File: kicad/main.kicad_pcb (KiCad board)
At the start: 2 copper layers, 130.7 x 94.9 mm, 40 parts

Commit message: wip: routing
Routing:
- net P2: track 92.2 -> 93.3 mm
- added copper zone on B.Cu, net GND

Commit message: chore: finish routing
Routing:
- net GND: track 909.2 -> 997.3 mm
- net RAW: track 12.7 -> 38.3 mm
- net RST: track 39.0 -> 51.5 mm, vias 0 -> 1
- net pos: track 49.6 -> 52.2 mm, vias 1 -> 2
- net P0: track 48.3 -> 49.2 mm
- net P15: track 151.5 -> 152.1 mm

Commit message: chore: straighten paths
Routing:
- net GND: track 997.3 -> 961.0 mm
- net P14: track 133.1 -> 138.2 mm
- net P16: track 107.9 -> 110.3 mm
- net P15: track 152.1 -> 153.7 mm
- net P9: track 133.8 -> 134.5 mm
- net P4: track 138.9 -> 139.6 mm
- net P10: track 83.9 -> 83.3 mm

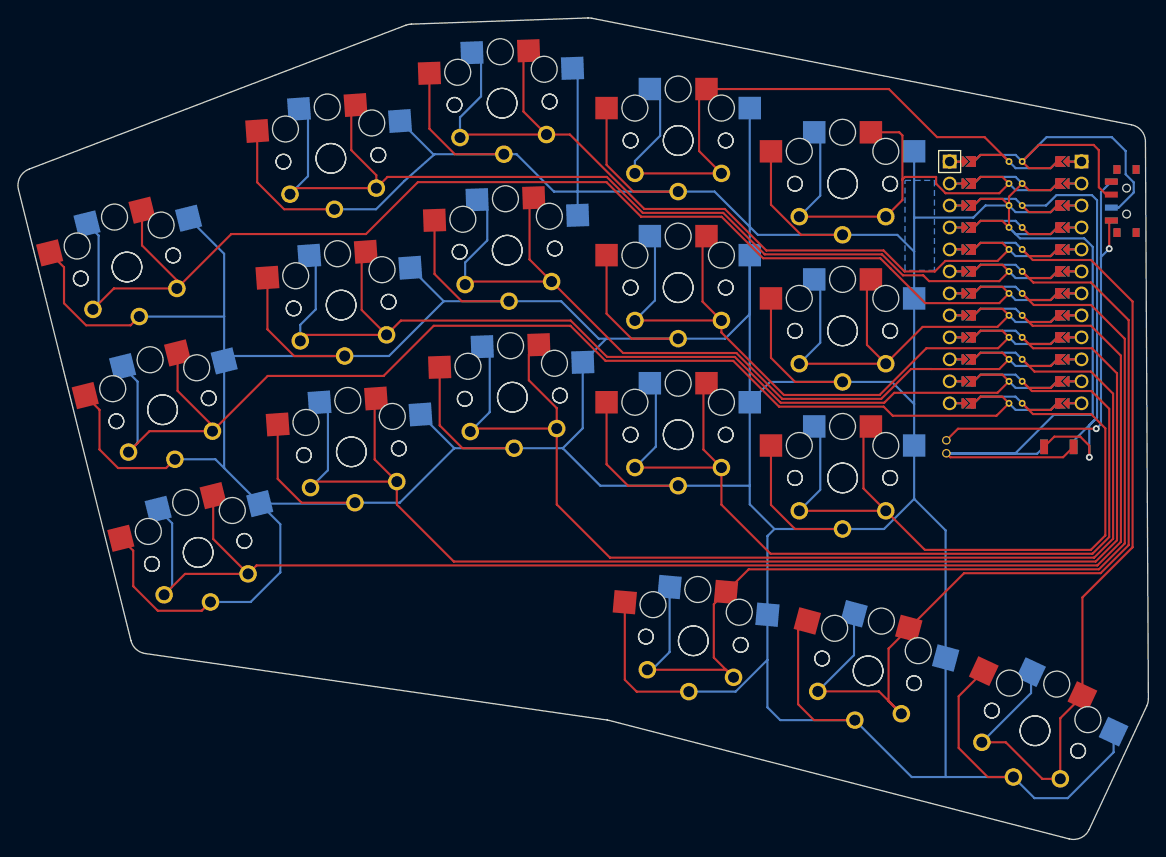
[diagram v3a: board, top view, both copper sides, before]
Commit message: feat: teardrops
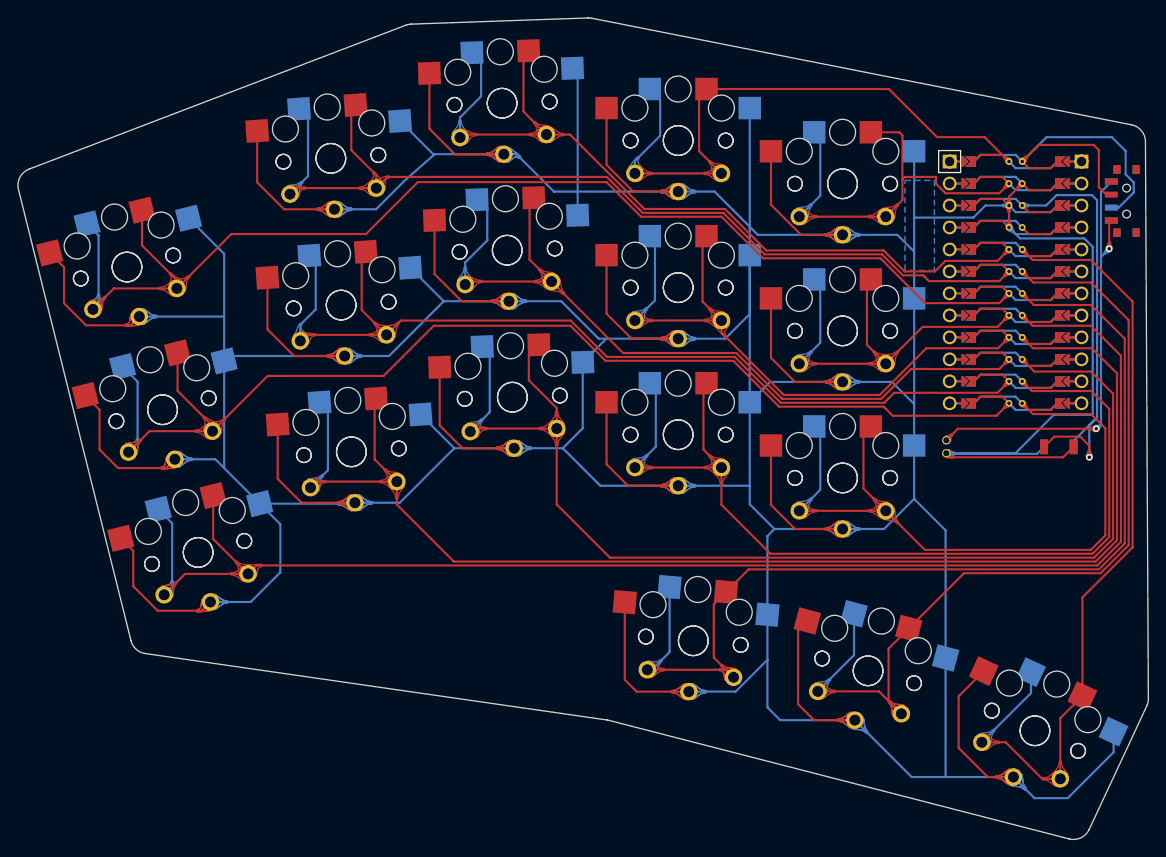
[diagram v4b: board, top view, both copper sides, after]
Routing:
- net P2: track 93.5 -> 90.7 mm
- net P10: track 83.3 -> 81.1 mm
- net P3: track 111.5 -> 109.4 mm
- net GND: track 961.0 -> 959.2 mm
- net P8: track 109.7 -> 108.0 mm
- net P14: track 138.2 -> 136.5 mm
- net P5: track 48.4 -> 46.8 mm
- net P15: track 153.7 -> 152.1 mm
- net P6: track 72.2 -> 70.7 mm
- net P16: track 110.3 -> 108.8 mm
- net P1: track 71.1 -> 69.9 mm
- net P7: track 92.8 -> 91.6 mm
- net P0: track 49.2 -> 48.2 mm
- net RST: track 51.5 -> 50.8 mm
- net P9: track 134.5 -> 133.8 mm
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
